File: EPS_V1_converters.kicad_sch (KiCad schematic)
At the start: 16 parts, among them U2 TPS62132RGTR, U3 TPS62133RGTR

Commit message: Minor fixes
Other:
- note added: "todo: add buck converter for 7.2V"
- note removed: "todo: add buck converter for 7.8V"
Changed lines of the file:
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@@
 	(generator_version "9.0")
 	(paper "A4")
-	(text "todo: add buck converter for 7.8V"
+	(text "todo: add buck converter for 7.2V"
 		(exclude_from_sim no)
 		(at 83.82 82.296 0)

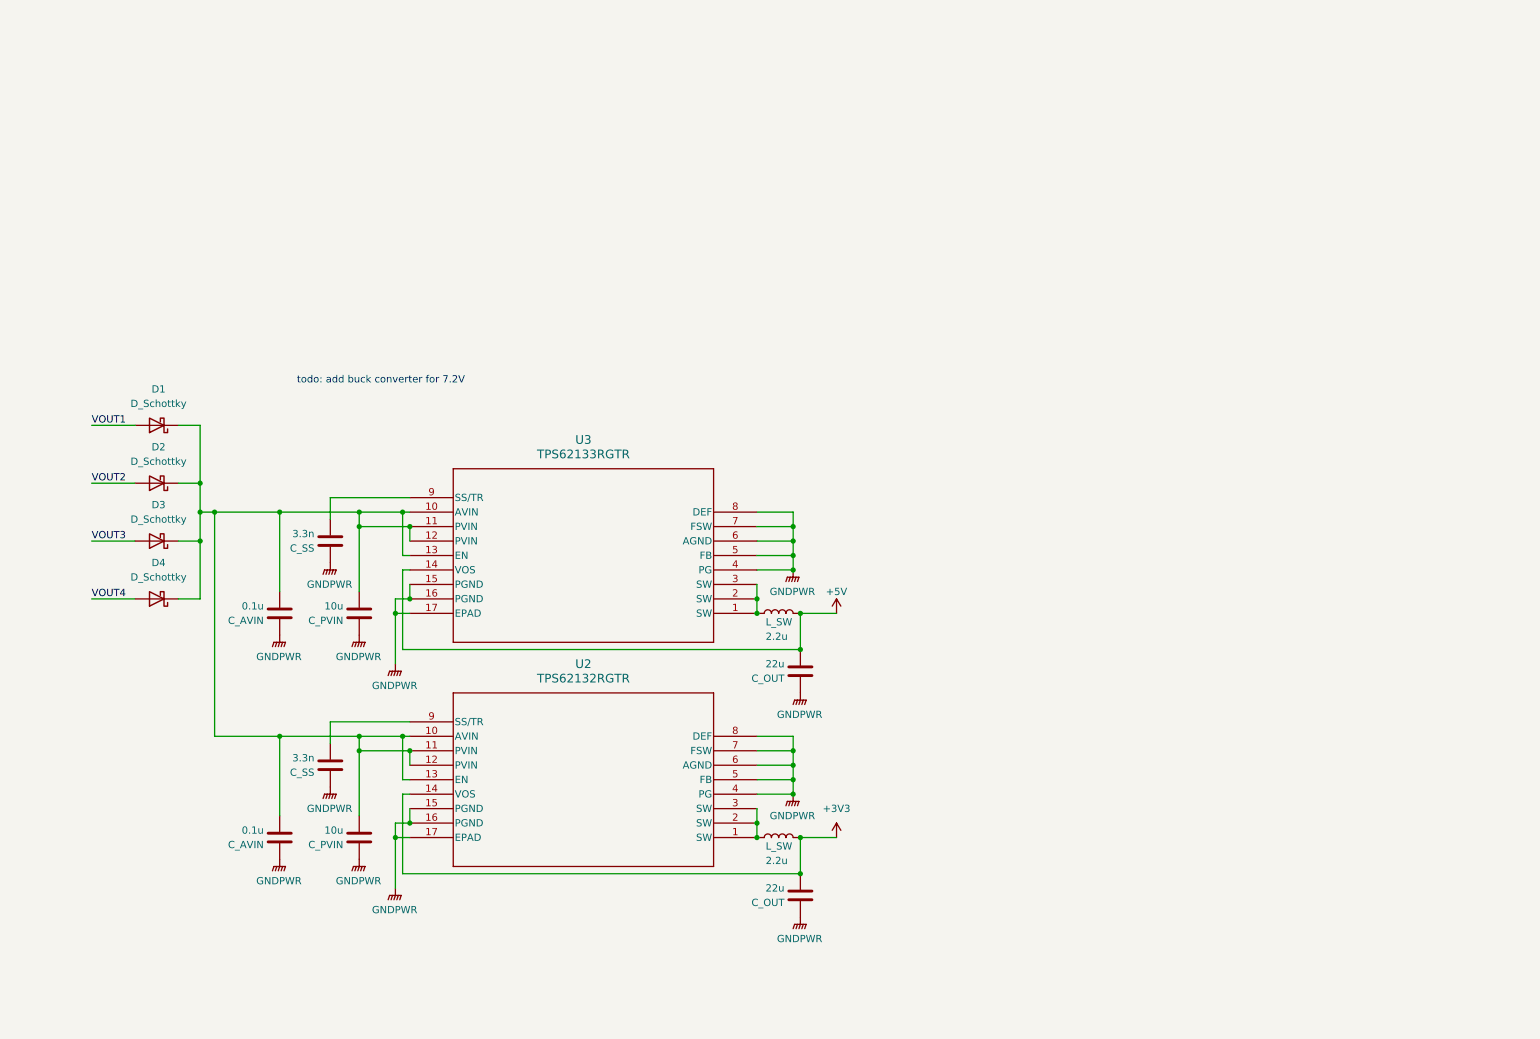
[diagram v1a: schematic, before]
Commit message: Add solar to charger buck-boost converter, make charger standalone instead of host control
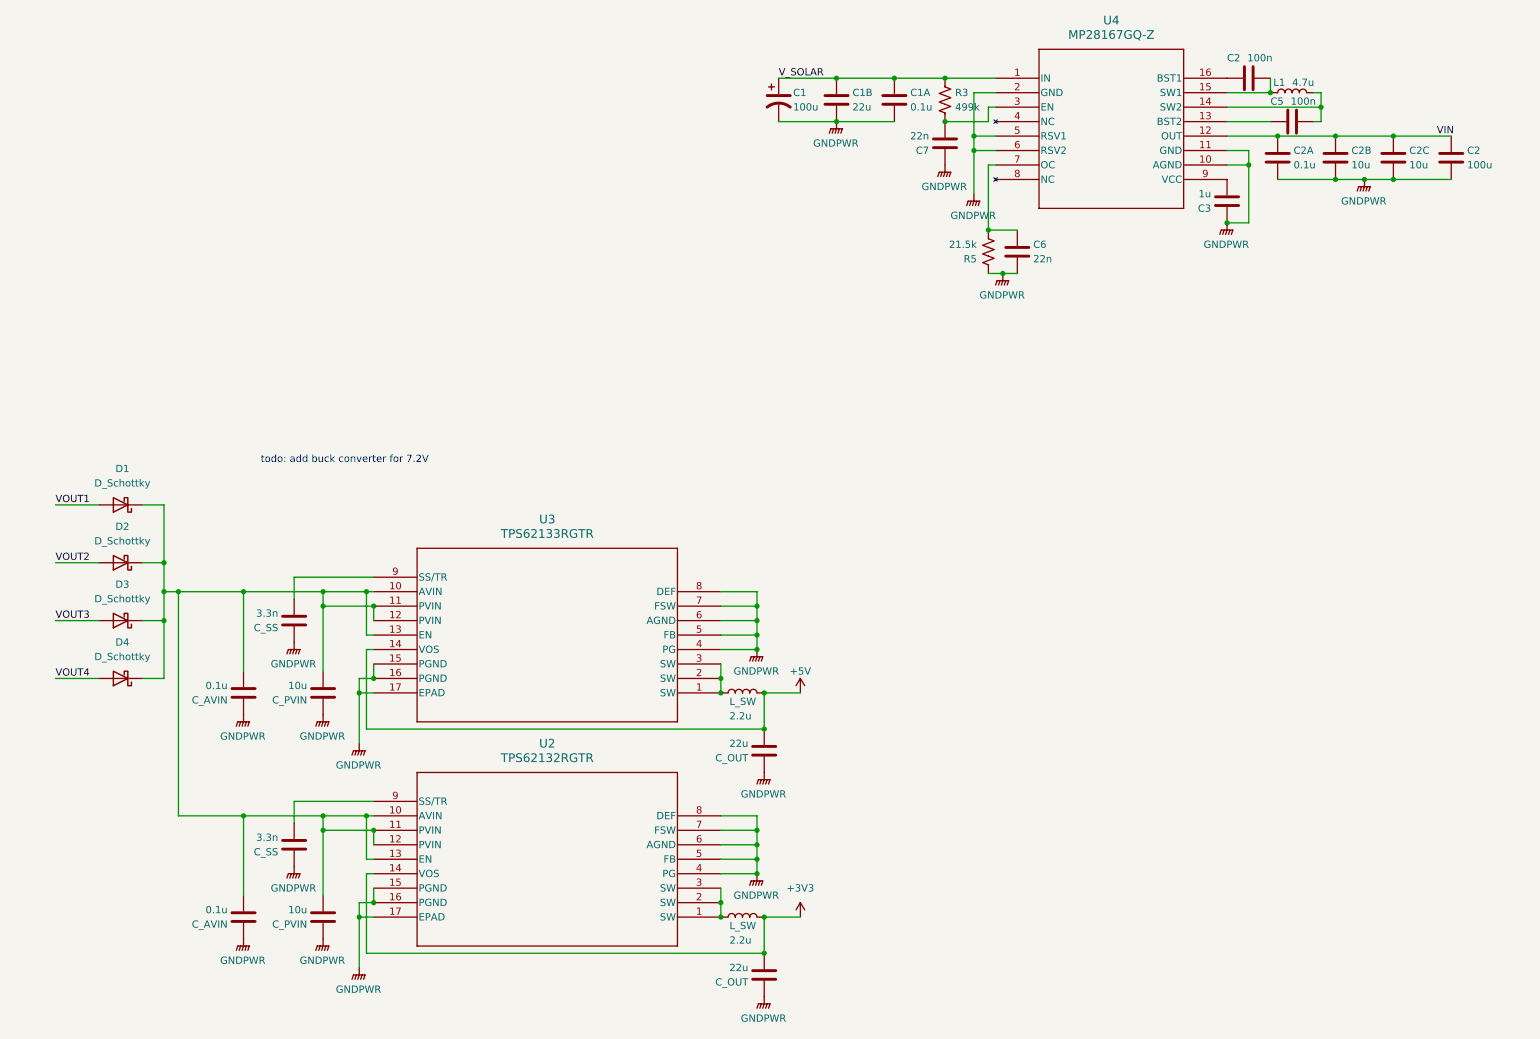
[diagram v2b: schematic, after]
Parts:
- added C1: 100u, symbol Device:C_Polarized_US
- added C1A, C2A: 0.1u, symbol Device:C
- added C1B: 22u, symbol Device:C
- added C2, C5: 100n, symbol Device:C
- added C2: 100u, symbol Device:C
- added C2B, C2C: 10u, symbol Device:C
- added C3: 1u, symbol Device:C
- added C6, C7: 22n, symbol Device:C
- added L1: 4.7u, symbol Device:L
- added R3: 499k, symbol Device:R_US
- added R5: 21.5k, symbol Device:R_US
- added U4: MP28167GQ-Z, QFN-16_MP28167GQ_MNP, symbol MP28167GQ-Z:MP28167GQ-Z
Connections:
- net GNDPWR: now also C1.2, C1A.2, C1B.2, C2.2, C2A.2, C2B.2, C2C.2, C3.1, C6.2, C7.1, R5.1, U4.10 (AGND), U4.11 (GND), U4.2 (GND), U4.5 (RSV1), U4.6 (RSV2)
- new net: C3.2, U4.9 (VCC)
- new net: C2.1, U4.16 (BST1)
- new net: C2.2, L1.1, U4.15 (SW1)
- new net: C7.2, R3.2, U4.3 (EN)
- new net: C5.1, U4.13 (BST2)
- new net: C5.2, L1.2, U4.14 (SW2)
- new net: C6.1, R5.2, U4.7 (OC)
- new net VIN: C2.1, C2A.1, C2B.1, C2C.1, U4.12 (OUT)
- new net V_SOLAR: C1.1, C1A.1, C1B.1, R3.1, U4.1 (IN)
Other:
- moved on the sheet: C_AVIN, C_OUT, C_PVIN, C_SS, D1, D2, D3, D4, L_SW, U2, U3

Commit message: Add fuel gauge, fix voltage labels
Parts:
- U2: footprint RGT16_1P7X1P7 -> TPS62132RGTR:RGT16_1P7X1P7
- U3: footprint RGT0016C -> TPS62133RGTR:RGT0016C
- U4: footprint QFN-16_MP28167GQ_MNP -> MP28167GQ-Z:QFN-16_MP28167GQ_MNP

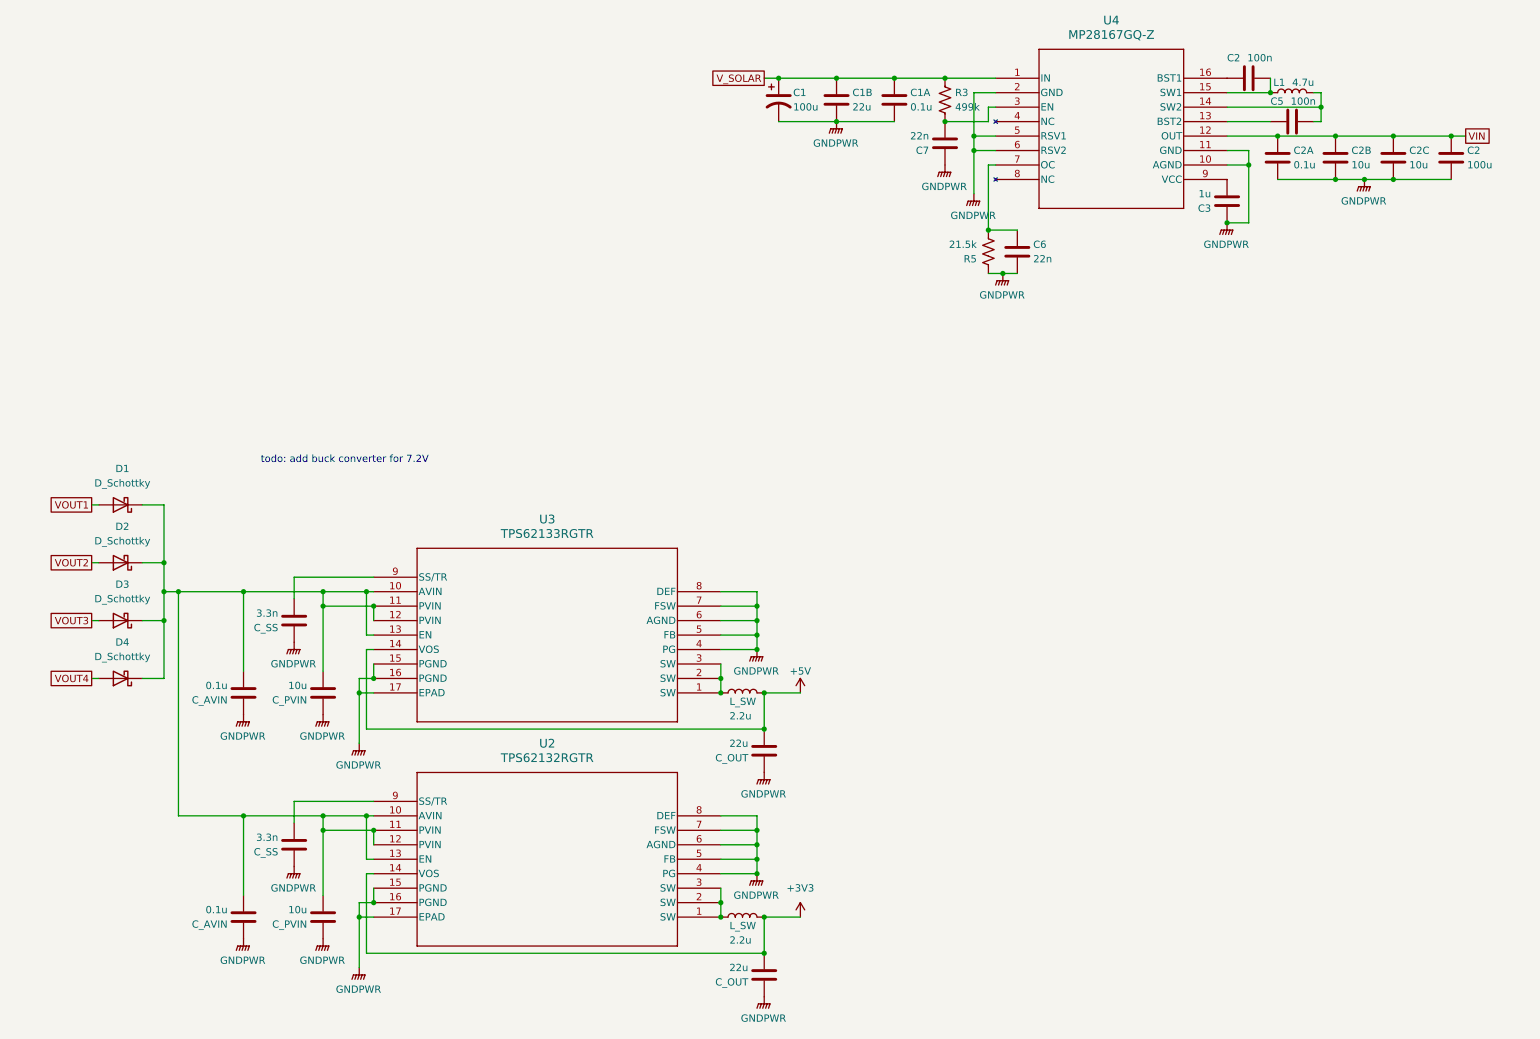
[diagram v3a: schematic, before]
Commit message: Add boost converter to 12V, fix grounding
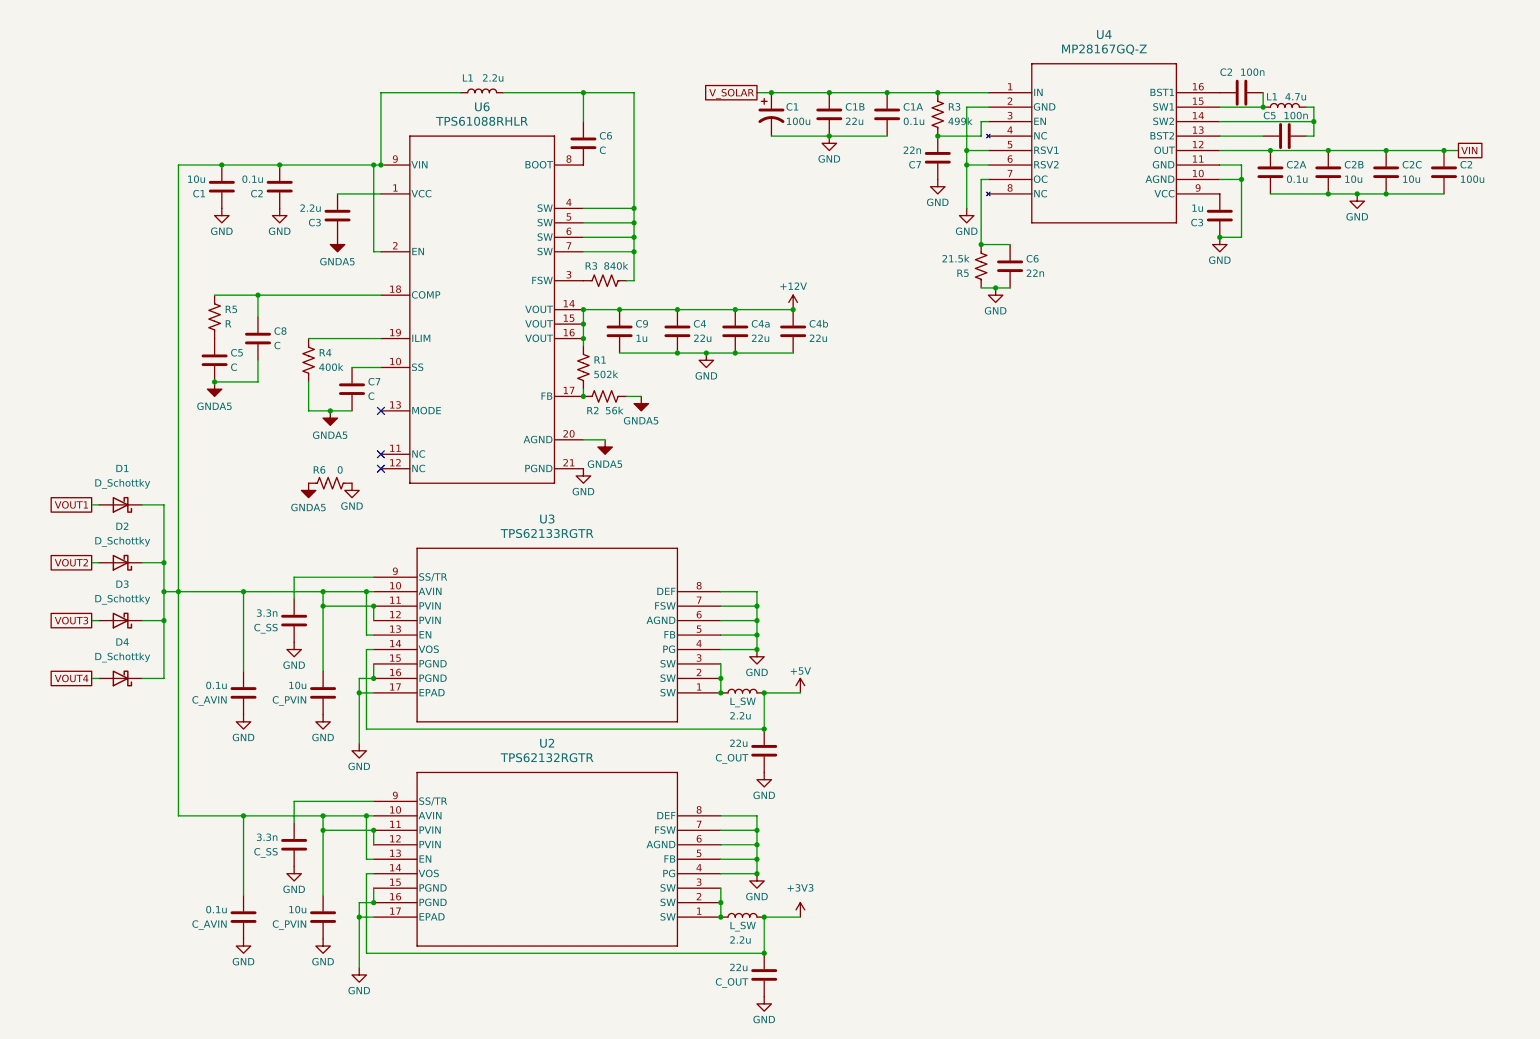
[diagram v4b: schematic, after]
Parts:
- added C1: 10u, symbol Device:C
- added C2: 0.1u, symbol Device:C
- added C3: 2.2u, symbol Device:C
- added C4, C4a, C4b: 22u, symbol Device:C
- added C5, C6, C7, C8: C, symbol Device:C
- added C9: 1u, symbol Device:C
- added L1: 2.2u, symbol Device:L
- added R1: 502k, symbol Device:R_US
- added R2: 56k, symbol Device:R_US
- added R3: 840k, symbol Device:R_US
- added R4: 400k, symbol Device:R_US
- added R5: R, symbol Device:R_US
- added R6: 0, symbol Device:R_US
- added U6: TPS61088RHLR, RHL0020A, symbol TPS61088RHLR:TPS61088RHLR
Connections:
- net at C_AVIN.2, C_AVIN.2, C_PVIN.2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: now also C1.2, C2.2, L1.1, U6.2 (EN), U6.9 (VIN)
- net GNDPWR renamed GND
- net GND: now also C1.1, C2.1, C4.2, C4a.2, C4b.2, C9.2, R6.2, U6.21 (PGND)
- new net: C4.1, C4a.1, C4b.1, C9.1, R1.1, U6.14 (VOUT), U6.15 (VOUT), U6.16 (VOUT)
- new net: C5.1, R5.2
- new net: C8.1, R5.1, U6.18 (COMP)
- new net: R3.1, U6.3 (FSW)
- new net: C6.1, L1.2, R3.2, U6.4 (SW), U6.5 (SW), U6.6 (SW), U6.7 (SW)
- new net: C3.2, U6.1 (VCC)
- new net: C7.1, U6.10 (SS)
- new net: R1.2, R2.2, U6.17 (FB)
- new net: R4.1, U6.19 (ILIM)
- new net: C6.2, U6.8 (BOOT)
- new net GNDA5: C3.1, C5.2, C7.2, C8.2, R2.1, R4.2, R6.1, U6.20 (AGND)
- no-connect marks 0 -> 3
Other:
- note removed: "todo: add buck converter for 7.2V"
- moved on the sheet: C1, C1A, C1B, C2, C2A, C2B, C2C, C3, C5, C6, C7, L1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

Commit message: Add 12V boost values
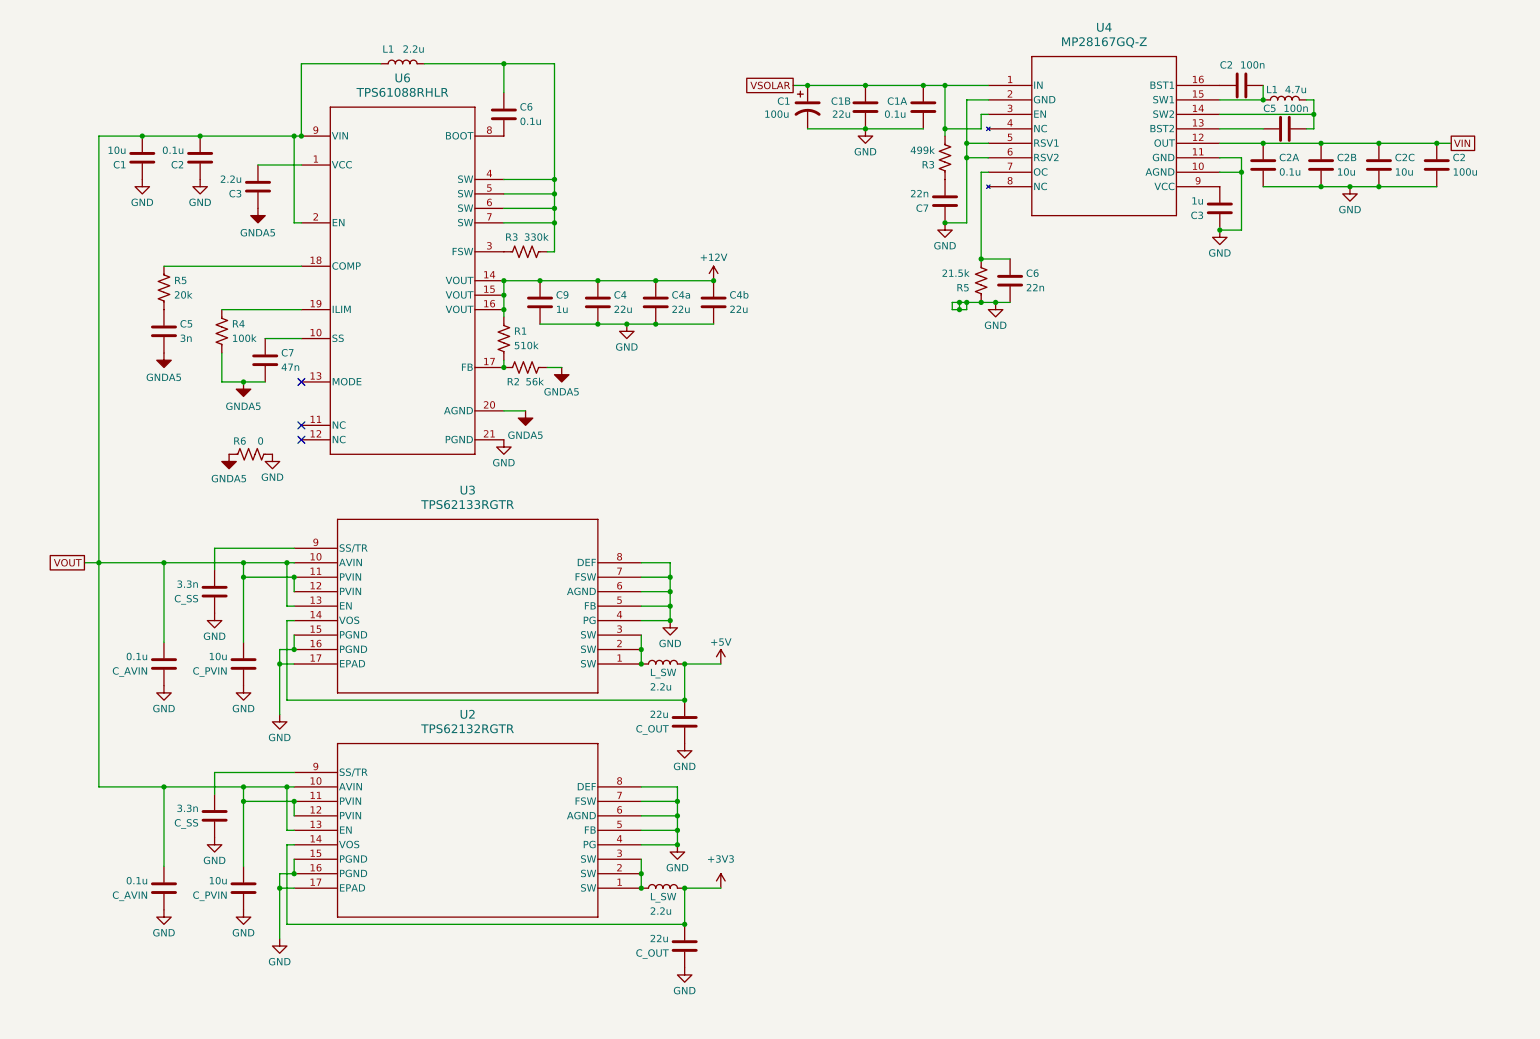
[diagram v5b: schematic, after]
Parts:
- removed C8: C, symbol Device:C
- removed D1, D2, D3, D4: D_Schottky, symbol Device:D_Schottky
- C5: value C -> 3n
- C6: value C -> 0.1u
- C7: value C -> 47n
- R1: value 502k -> 510k
- R3: value 840k -> 330k
- R4: value 400k -> 100k
- R5: value R -> 20k
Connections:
- net GND: now also C1B.1; no longer C1B.2
- net VOUT: now reaches C1.2, C2.2, C_AVIN.2, C_AVIN.2, C_PVIN.2, C_PVIN.2, L1.1, U2.10 (AVIN), U2.11 (PVIN), U2.12 (PVIN), U2.13 (EN), U3.10 (AVIN), U3.11 (PVIN), U3.12 (PVIN), U3.13 (EN), U6.2 (EN), U6.9 (VIN)
- net VSOLAR: now reaches R3.2, U4.3 (EN)
- net VSOLAR: now also C1.1, C1A.1, C1B.2, U4.1 (IN); no longer C7.2
- removed net V_SOLAR: C1.1, C1A.1, C1B.1, R3.1, U4.1 (IN)
- new net: C7.2, R3.1
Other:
- moved on the sheet: C1, C1A, C1B, C2, C2A, C2B, C2C, C3, C4, C4a, C4b, C5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

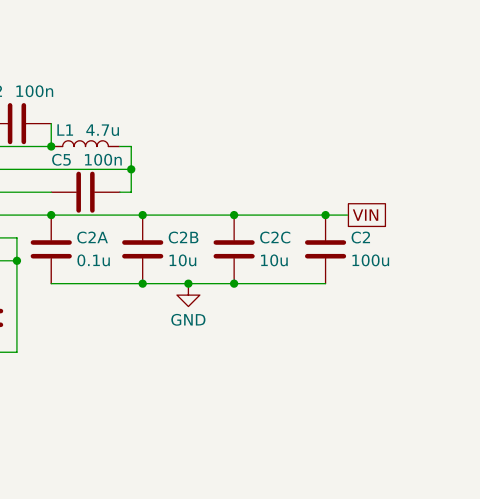
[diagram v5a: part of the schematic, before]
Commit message: Add 5V charging input
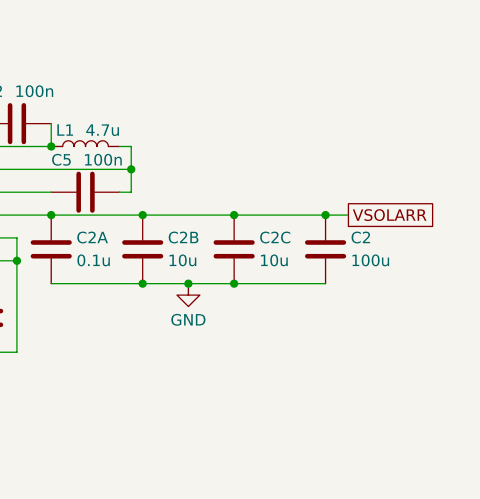
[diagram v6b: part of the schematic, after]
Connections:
- net VIN renamed VSOLARR
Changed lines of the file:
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@@
 		)
 	)
-	(global_label "VIN"
+	(global_label "VSOLARR"
 		(shape passive)
 		(at 271.78 40.64 0)
@@
 		)
 		(property "Intersheetrefs" "${INTERSHEET_REFS}"
-			(at 276.6778 40.64 0)
+			(at 281.9392 40.64 0)
 			(effects
 				(font
